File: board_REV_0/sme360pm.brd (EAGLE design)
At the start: 45 x 80 mm, 56 parts, among them J1 USB3075-30-A, P1 HEADER, P2 JTAG, SW1 TL3342F160QG/TR, U1 RT9193-33GB, U2 STM32F103C8T6, U3 MCP2551-I/SN, X1 87438-03, X2 87438-03, X3 87438-03, X4 87438-03, Y2 8MHz, Y3 32.768k

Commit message: Updated board
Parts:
- moved R19 18.0 mm to (14.4, 30.8), turned to 90 degrees
- moved R18 17.9 mm to (14.4, 34.3)
- moved R20 17.2 mm to (21.0, 23.6)
- moved R21 17.1 mm to (24.6, 23.6)
- moved R17 15.6 mm to (24.6, 40.8), turned to 180 degrees
- moved R15 14.6 mm to (30.9, 33.8), turned to 270 degrees
- moved R16 9.31 mm to (20.9, 40.8), turned to 180 degrees
- moved R14 7.61 mm to (30.9, 30.2), turned to 270 degrees
- moved C14 3.73 mm to (23.1, 42.3)
- moved C13 0.09 mm to (18.6, 42.3)
- turned C12 to 0 degrees
- turned C18 to 0 degrees
- turned PC13 to 270 degrees
- renumbered X1 to ENC1, X2 to ENC2, X3 to ENC3, X4 to ENC4
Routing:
- net 3.3V: track 147.8 -> 97.7 mm, vias 5 -> 4
- net N$19: track 29.5 -> 62.8 mm, vias 0 -> 2
- net N$16: track 27.3 -> 59.5 mm, vias 0 -> 2
- net VCC: track 188.6 -> 157.6 mm, vias 6 -> 2
- net PA12: track 80.4 -> 53.5 mm, vias 2 -> 1
- net PC14: track 50.9 -> 26.7 mm
- net PC13: track 47.5 -> 24.1 mm, vias 1 -> 3
- net GND: track 308.7 -> 285.4 mm, vias 3 -> 9
- net PA2: track 28.3 -> 7.20 mm
- net N$18: track 40.8 -> 20.8 mm
- net N$1: track 44.8 -> 28.3 mm
- net SWDCLK: track 29.6 -> 43.3 mm, vias 0 -> 1
- net PA3: track 19.3 -> 6.97 mm
- net N$2: track 47.8 -> 38.0 mm
- net PA11: track 65.0 -> 55.6 mm, vias 2 -> 1
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- removed copper zone on layer 1, net GND
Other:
- board text added: "LNS - ENCODERS REV 1.230306 PABLO"

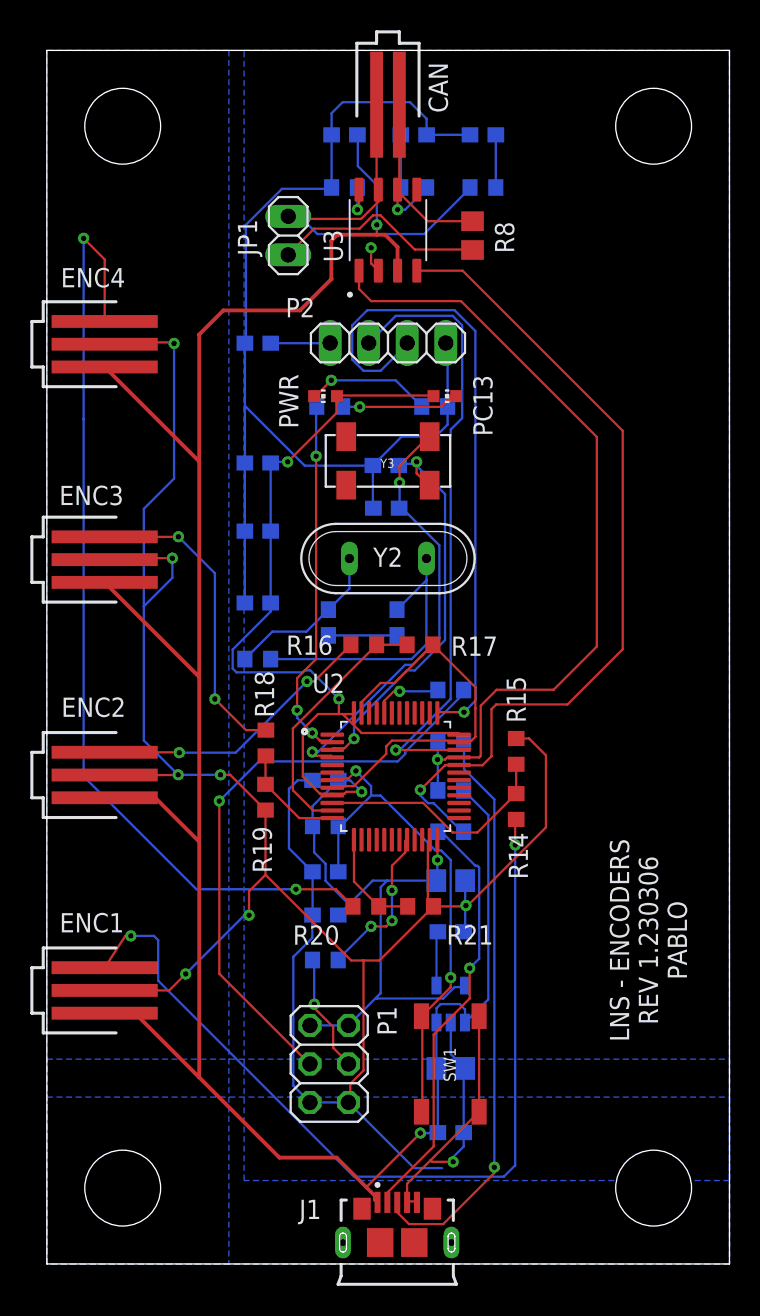
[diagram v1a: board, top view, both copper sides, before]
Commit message: Removed voltage divider
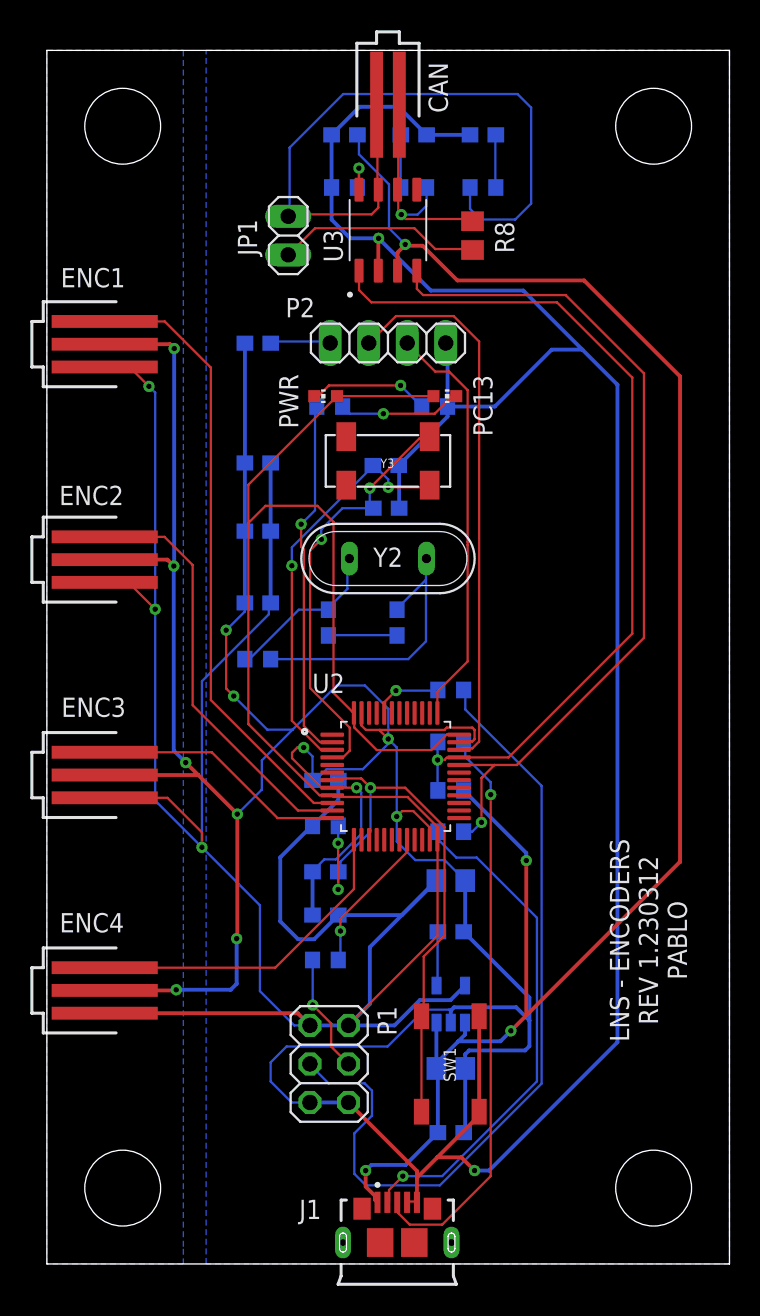
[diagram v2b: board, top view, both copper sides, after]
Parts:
- removed R14, R16, R18, R20: 10k, rcl:R0603
- removed R15, R17, R19, R21: 20k, rcl:R0603
- moved ENC1 42.6 mm to (3.81, 60.6)
- moved ENC4 42.6 mm to (3.81, 18.0)
- moved ENC2 14.2 mm to (3.81, 46.4)
- moved ENC3 14.2 mm to (3.81, 32.2)
- turned C12 to 180 degrees
- turned C9 to 180 degrees
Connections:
- removed net N$16: ENC1.1, R14.2
- removed net N$17: ENC2.1, R16.2
- removed net N$18: ENC3.1, R18.2
- removed net N$19: ENC4.1, R20.2
- net 3.3V: now also ENC1.3, ENC2.3, ENC3.3, ENC4.3
- net GND: no longer R15.1, R17.1, R19.1, R21.1
- net PA0: now also ENC1.1; no longer R14.1, R15.2
- net PA1: now also ENC2.1; no longer R16.1, R17.2
- net PA2: now also ENC3.1; no longer R18.1, R19.2
- net PA3: now also ENC4.1; no longer R20.1, R21.2
- net VCC: no longer ENC1.3, ENC2.3, ENC3.3, ENC4.3
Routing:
- net 3.3V: track 97.7 -> 240.4 mm, vias 4 -> 3
- net GND: track 285.4 -> 361.2 mm, vias 9 -> 14
- net N$19: track 62.8 -> 0.00 mm, vias 2 -> 0
- net N$16: track 59.5 -> 0.00 mm, vias 2 -> 0
- net VCC: track 157.6 -> 119.6 mm, vias 2 -> 4
- net PA0: track 15.9 -> 41.0 mm
- net N$13: track 26.7 -> 47.8 mm
- net N$18: track 20.8 -> 0.00 mm, vias 2 -> 0
- net N$17: track 19.2 -> 0.00 mm, vias 2 -> 0
- net SWDCLK: track 43.3 -> 27.4 mm, vias 1 -> 0
- net N$8: track 39.2 -> 54.4 mm, vias 1 -> 0
- net PA3: track 6.97 -> 21.8 mm
- net PA1: track 17.0 -> 27.9 mm
- net PA2: track 7.20 -> 16.8 mm
- net RESET: track 34.5 -> 40.0 mm, vias 2 -> 3
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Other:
- board text added: "LNS - ENCODERS REV 1.230312 PABLO"
- board text removed: "LNS - ENCODERS REV 1.230306 PABLO"
